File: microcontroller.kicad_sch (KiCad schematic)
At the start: 26 parts, among them IC14 PIC32MZ2048EFG064-E_PT

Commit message: first round of revisions
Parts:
- FB1, FB2, FB3, FB4: symbol SamacSys_Parts:BMC1JY0300AN -> Oro:FerriteBead
- IC14: Mouser Part Number (none) -> 579-MZ2048EFG064EPT; Mouser Price/Stock (none) -> https://www.mouser.de/ProductDetail/Microchip-Technology-At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
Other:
- moved on the sheet: FB1, FB2, FB3, FB4
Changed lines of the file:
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@@
+    (stroke (width 0) (type default))
+  )
+  (wire (pts (xy 256.54 93.98) (xy 267.97 93.98))
     (stroke (width 0) (type default))
   )
@@
     (stroke (width 0) (type default))
   )
-  (wire (pts (xy 215.9 93.98) (xy 224.79 93.98))
+  (wire (pts (xy 213.36 93.98) (xy 224.79 93.98))
     (stroke (width 0) (type default))
   )
@@
     (stroke (width 0) (type default))
   )
-  (wire (pts (xy 243.84 113.03) (xy 243.84 119.38))
+  (wire (pts (xy 243.84 110.49) (xy 243.84 119.38))
     (stroke (width 0) (type default))
   )
@@
     (stroke (width 0) (type default))
   )
-  (wire (pts (xy 200.66 113.03) (xy 200.66 119.38))
+  (wire (pts (xy 200.66 110.49) (xy 200.66 119.38))
     (stroke (width 0) (type default))
   )
@@
     (stroke (width 0) (type default))
   )
-  (wire (pts (xy 259.08 93.98) (xy 267.97 93.98))
-    (stroke (width 0) (type default))
-  )
   (wire (pts (xy 100.33 31.75) (xy 100.33 36.83))
     (stroke (width 0) (type default))
@@
     (fill (type none))
   )
+  (arc (start 248.92 99.06) (mid 249.292 98.162) (end 250.19 97.79)
+    (stroke (width 0) (type default))
+    (fill (type none))
+  )
+  (arc (start 248.92 101.6) (mid 248.548 102.498) (end 247.65 102.87)
+    (stroke (width 0) (type default))
+    (fill (type none))
+  )
   (rectangle (start 134.62 173.99) (end 135.89 173.99)
     (stroke (width 0) (type default))
@@
     (fill (type none))
   )
+  (arc (start 205.74 101.6) (mid 205.368 102.498) (end 204.47 102.87)
+    (stroke (width 0) (type default))
+    (fill (type none))
+  )
   (rectangle (start 135.89 173.99) (end 135.89 191.77)
     (stroke (width 0) (type default))
@@
   )
   (rectangle (start 220.98 116.84) (end 222.25 116.84)
+    (stroke (width 0) (type default))
+    (fill (type none))
+  )
+  (arc (start 205.74 99.06) (mid 206.112 98.162) (end 207.01 97.79)
     (stroke (width 0) (type default))
     (fill (type none))
@@
   (symbol (lib_id "SamacSys_Parts:01016D104KAT2A") (at 267.97 93.98 90) (mirror x) (unit 1)
     (in_bom yes) (on_board yes) (dnp no)
-    (property "Reference" "C16" (at 271.78 100.33 90)
-      (effects (font (size 1.27 1.27)) (justify right))
-    )
-    (property "Value" "0.1u" (at 274.32 102.87 90)
-      (effects (font (size 1.27 1.27)) (justify left))
+    (property "Reference" "C16" (at 269.24 104.14 90)
+      (effects (font (size 1.27 1.27)) (justify right bottom))
+    )
+    (property "Value" "0.1u" (at 269.24 104.14 90)
+      (effects (font (size 1.27 1.27)) (justify right top))
     )
     (property "Footprint" "SamacSys_Parts:CAPC0402X22N" (at 266.7 102.87 0)
@@
     )
   )
-  (symbol (lib_name "BMC1JY0300AN_1") (lib_id "SamacSys_Parts:BMC1JY0300AN") (at 200.66 93.98 0) (unit 1)
+  (symbol (lib_id "Oro:FerriteBead") (at 200.66 93.98 0) (unit 1)
     (in_bom yes) (on_board yes) (dnp no)
-    (property "Reference" "FB1" (at 213.36 95.25 0)
-      (effects (font (size 1.27 1.27)))
-    )
-    (property "Value" "BMC1JY0300AN" (at 210.82 99.06 0)
+    (property "Reference" "FB1" (at 209.55 96.52 0)
+      (effects (font (size 1.27 1.27)))
+    )
+    (property "Value" "BMC1JY0300AN" (at 209.55 100.33 0)
       (effects (font (size 1.27 1.27)))
     )
@@
     )
   )
-  (symbol (lib_name "BMC1JY0300AN_1") (lib_id "SamacSys_Parts:BMC1JY0300AN") (at 243.84 93.98 0) (unit 1)
+  (symbol (lib_id "Oro:FerriteBead") (at 243.84 93.98 0) (unit 1)
     (in_bom yes) (on_board yes) (dnp no)
-    (property "Reference" "FB3" (at 256.54 95.25 0)
-      (effects (font (size 1.27 1.27)))
-    )
-    (property "Value" "BMC1JY0300AN" (at 254 99.06 0)
+    (property "Reference" "FB3" (at 252.73 96.52 0)
+      (effects (font (size 1.27 1.27)))
+    )
+    (property "Value" "BMC1JY0300AN" (at 252.73 100.33 0)
       (effects (font (size 1.27 1.27)))
     )
@@
   (symbol (lib_id "SamacSys_Parts:01016D104KAT2A") (at 224.79 93.98 90) (mirror x) (unit 1)
     (in_bom yes) (on_board yes) (dnp no)
-    (property "Reference" "C16" (at 228.6 100.33 90)
-      (effects (font (size 1.27 1.27)) (justify right))
-    )
-    (property "Value" "0.1u" (at 232.41 102.87 90)
-      (effects (font (size 1.27 1.27)) (justify left))
+    (property "Reference" "C16" (at 226.06 104.14 90)
+      (effects (font (size 1.27 1.27)) (justify right bottom))
+    )
+    (property "Value" "0.1u" (at 226.06 104.14 90)
+      (effects (font (size 1.27 1.27)) (justify right top))
     )
     (property "Footprint" "SamacSys_Parts:CAPC0402X22N" (at 223.52 102.87 0)
@@
     )
   )
-  (symbol (lib_name "BMC1JY0300AN_1") (lib_id "SamacSys_Parts:BMC1JY0300AN") (at 243.84 97.79 270) (unit 1)
+  (symbol (lib_id "Oro:FerriteBead") (at 243.84 97.79 270) (unit 1)
     (in_bom yes) (on_board yes) (dnp no)
-    (property "Reference" "FB4" (at 246.38 105.41 90)
-      (effects (font (size 1.27 1.27)) (justify left))
+    (property "Reference" "FB4" (at 247.65 105.41 90)
+      (effects (font (size 1.27 1.27)))
     )
     (property "Value" "BMC1JY0300AN" (at 234.4634 102.2953 90)
@@
       (effects (font (size 1.27 1.27)) (justify left) hide)
     )
-    (property "Mouser Part Number" "" (at 175.26 45.72 0)
-      (effects (font (size 1.27 1.27)) (justify left) hide)
-    )
-    (property "Mouser Price/Stock" "" (at 175.26 48.26 0)
+    (property "Mouser Part Number" "579-MZ2048EFG064EPT" (at 175.26 45.72 0)
+      (effects (font (size 1.27 1.27)) (justify left) hide)
+    )
+    (property "Mouser Price/Stock" "https://www.mouser.de/ProductDetail/Microchip-Technology-Atmel/PIC32MZ2048EFG064-E-PT?qs=r%2FmwOkjQ8utX5RH6pDxK9w%3D%3D" (at 175.26 48.26 0)
       (effects (font (size 1.27 1.27)) (justify left) hide)
     )
@@
     )
   )
-  (symbol (lib_name "BMC1JY0300AN_1") (lib_id "SamacSys_Parts:BMC1JY0300AN") (at 200.66 97.79 270) (unit 1)
+  (symbol (lib_id "Oro:FerriteBead") (at 200.66 97.79 270) (unit 1)
     (in_bom yes) (on_board yes) (dnp no)
-    (property "Reference" "FB2" (at 203.2 105.41 90)
-      (effects (font (size 1.27 1.27)) (justify left))
+    (property "Reference" "FB2" (at 204.47 105.41 90)
+      (effects (font (size 1.27 1.27)))
     )
     (property "Value" "BMC1JY0300AN" (at 191.2834 102.2953 90)

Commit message: begin refactor for rev3
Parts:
- added C16 (x8): 0.1u, SamacSys_Parts:CAPC0402X22N, symbol SamacSys_Parts:01016D104KAT2A
- added C21: 1u, SamacSys_Parts:CAPC1608X90N, symbol SamacSys_Parts:0603YD105KAT2A
- added C22: 4.7u, SamacSys_Parts:CAPC2012X135N, symbol SamacSys_Parts:CL21A475KOFNNNE
- added C68, C69, C71: 2.2u, CAPC1608X90N, symbol SamacSys_Parts:CL10A225KP8NNNC
- added IC8: STM32F479VGT6, QFP50P1600X1600X160-100N, symbol SamacSys_Parts:STM32F479VGT6
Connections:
- net VDD1 is gone; now on net +3V3: C16.2, C16.2, C16.2, FB2.2, IC14.54 (VDD_4), IC14.60 (VDD_5), IC14.8 (VDD_1)
- net VDD2 is gone; now on net +3V3: C16.2, C16.2, C16.2, FB4.2, IC14.26 (VDD_2), IC14.34 (VUSB3V3), IC14.39 (VDD_3)
- net +3V3: now also C16.2, C16.2, C16.2, C16.2, C16.2, C16.2, C16.2, C16.2, C21.2, C22.1, C71.1, IC8.100 (VDD_5), IC8.17 (VREF+), IC8.18 (VDDA), IC8.24 (VDD_2), IC8.3 (VBAT), IC8.45 (VDD_3), IC8.55 (VDDDSI), IC8.56 (VCAPDSI), IC8.62 (VDD12DSI), IC8.65 (VDDUSB), IC8.77 (VDD_4), IC8.8 (VDD_1)
- net ETH_~{RST}: now also IC8.4 (PC13)
- net GND: now also C16.1, C16.1, C16.1, C16.1, C16.1, C16.1, C16.1, C16.1, C21.1, C22.2, C68.2, C69.2, C71.2, IC8.16 (VSSA), IC8.2 (VSS_1), IC8.23 (VSS_3), IC8.44 (VSS_4), IC8.59 (VSSDSI), IC8.7 (VSS_2), IC8.78 (VSS_5)
- new net VCAP1: C68.1, IC8.43 (VCAP1)
- new net VCAP2: C69.1, IC8.76 (VCAP2)
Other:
- note added: "TODO: OSCILLATOR"
- moved on the sheet: C16, FB1, FB2, FB3, FB4, IC14, R19, R43

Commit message: fully move to new MCU configuration
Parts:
- removed C16 (x10): 0.1u, SamacSys_Parts:CAPC0402X22N, symbol SamacSys_Parts:01016D104KAT2A
- removed FB1, FB2, FB3, FB4: BMC1JY0300AN, BEADC1608X95N, symbol Oro:FerriteBead
- removed IC14: PIC32MZ2048EFG064-E_PT, SamacSys_Parts:QFP50P1200X1200X120-64N, symbol SamacSys_Parts:PIC32MZ2048EFG064-E_PT
- removed R43 (x9): 10k, RESC5025X65N, symbol SamacSys_Parts:RC2010JK-0710KL
- added LED5: AA3528VRVFS/A, SamacSys_Parts:AA3528VRVFSA, symbol SamacSys_Parts:AA3528VRVFS_A
- added R10: 10k, SamacSys_Parts:RESC5025X65N, symbol SamacSys_Parts:RC2010JK-0710KL
- added R5: 1k, RESC2012X60N, symbol SamacSys_Parts:SG73P2ATTD102J
- renumbered C71 to C11, C68 to C2, C69 to C3, IC8 to IC1, R19 to R1, R19 to R2
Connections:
- net ETH_~{RST} is gone; now on net EXTETH_~{RST}: IC1.4 (PC13)
- net +3V3: now also LED5.2, R10.1
- net EXTETH_SCK: now also IC1.41 (PB10)
- net I2C_SCL: now also IC1.95 (PB6)
- net I2C_SDA: now also IC1.96 (PB7)
- net OLED_SCK: now also IC1.81 (PC10)
- net OLED_~{RST}: now also IC1.89 (PD5)
- net USB_D+: now also IC1.74 (PA12)
- net USB_D-: now also IC1.73 (PA11)
- net EXTETH_MISO: now reaches IC1.14 (PC2)
- net EXTETH_MOSI: now reaches IC1.15 (PC3)
- net SYSUART_RTS: now reaches IC1.20 (PA1)
- net SYSUART_TX: now reaches IC1.21 (PA2)
- net SYSUART_RX: now reaches IC1.22 (PA3)
- net SYSETH_SCK: now reaches IC1.26 (PA5)
- net SYSETH_MISO: now reaches IC1.27 (PA6)
- net SYSTEH_MOSI: now reaches IC1.28 (PA7)
- net SYSTEH_~{RST}: now reaches IC1.29 (PB0)
- net SYSTEH_~{INT}: now reaches IC1.30 (PB1)
- net DBGUART_RX: now reaches IC1.32 (PE7)
- net DBGUART_TX: now reaches IC1.33 (PE8)
- net at IC1.37 (PE12): now also R5.1
- net PSU_ON: now reaches IC1.47 (PB13)
- net PSU_OK: now reaches IC1.48 (PB14)
- net SYS_RESET: now reaches IC1.49 (PB15)
- net SYS_POWER: now reaches IC1.50 (PD8)
- net SWDIO: now reaches IC1.75 (PA13)
- net SWCLK: now reaches IC1.79 (PA14)
- net SYSUART_CTS: now reaches IC1.87 (PD3)
- net OLED_MOSI: now reaches IC1.90 (PD6)
- net SWO: now reaches IC1.92 (PB3)
- net ~{FLASH}: now reaches IC1.97 (BOOT0)
- net ~{FLASH}: now also R10.2
- net EXTETH_~{INT}: now reaches IC1.99 (PB9)
- new net: LED5.1, R5.2
- no-connect marks 0 -> 44
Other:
- note removed: "10k"
- moved on the sheet: R1, R2

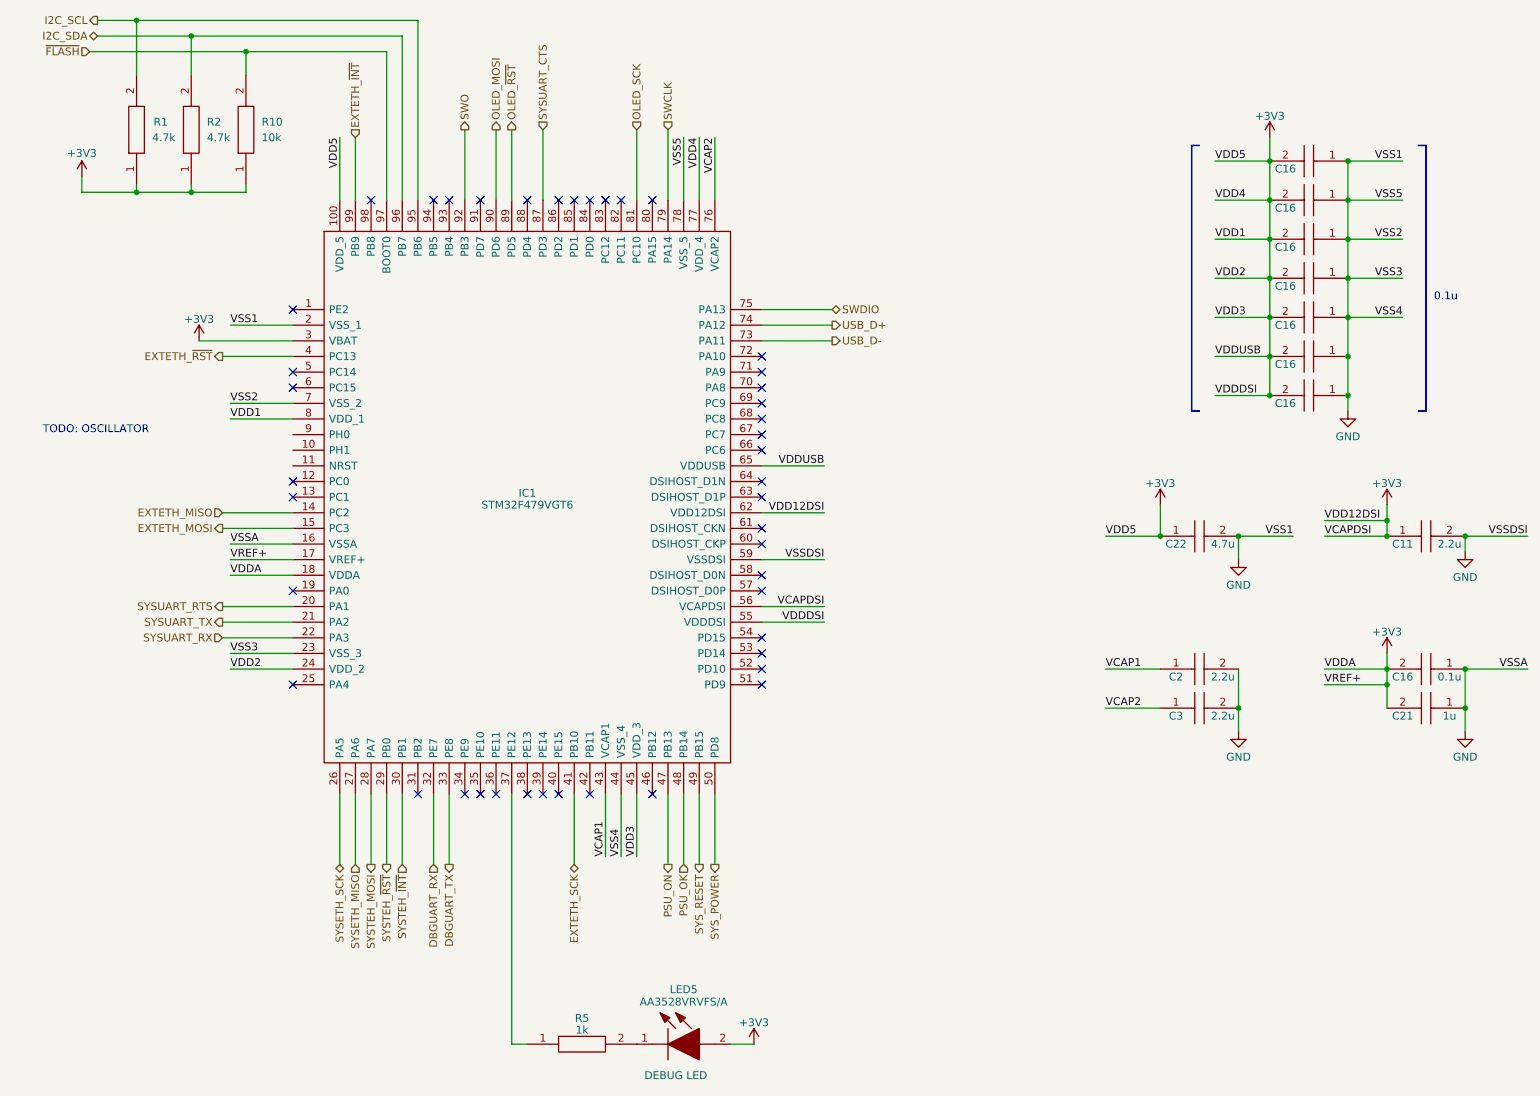
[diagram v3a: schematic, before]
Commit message: first few boards laid out
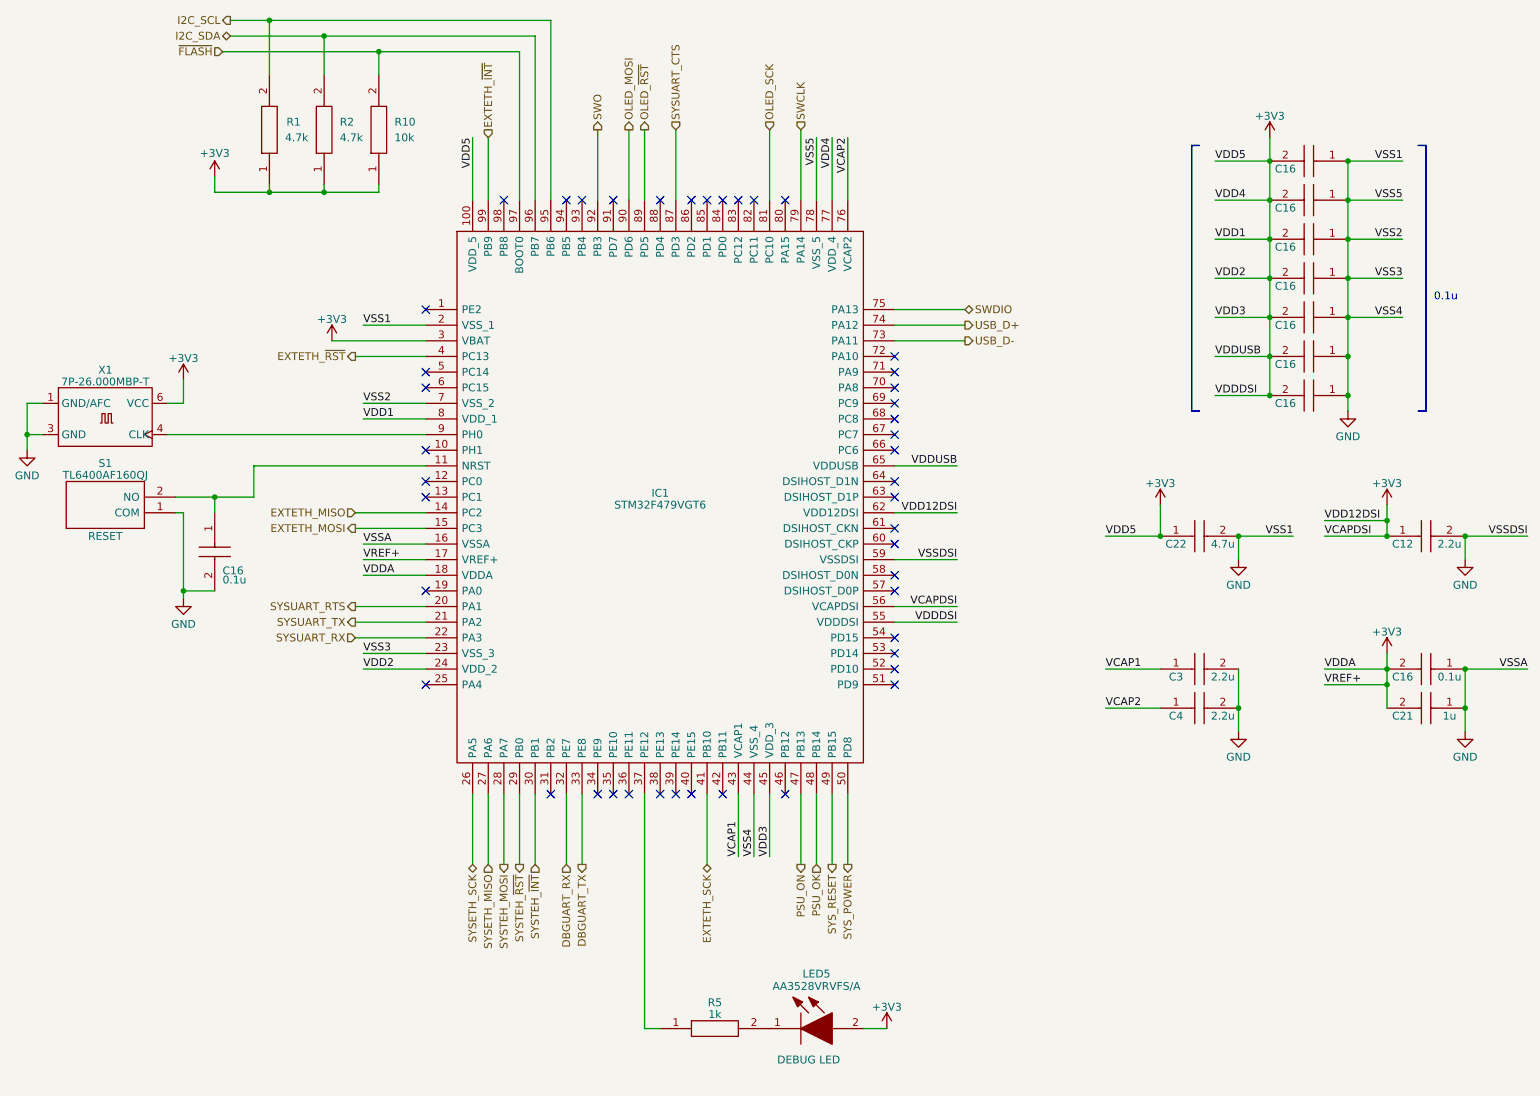
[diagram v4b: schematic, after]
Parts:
- added C16: 0.1u, SamacSys_Parts:CAPC0402X22N, symbol SamacSys_Parts:GRT31C5C1H104FA02L
- added S1: TL6400AF160QJ, TL6400AF160QJ, symbol SamacSys_Parts:TL6400AF160QJ
- added X1: 7P-26.000MBP-T, Oro Footprints:7P-26.000MBP-T, symbol Oro:7P-26.000MBP-T
- C16: symbol SamacSys_Parts:01016D104KAT2A -> SamacSys_Parts:GRT31C5C1H104FA02L
- R1, R2: symbol SamacSys_Parts:MCWR04X4701FTL -> SamacSys_Parts:RC2512FK-074K7L; Arrow Part Number (none) -> RC2512FK-074K7L; Arrow Price/Stock (none) -> https://www.arrow.com/en/products/rc2512fk-074k7l/yageo?reg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; Mouser Part Number (none) -> 603-RC2512FK-074K7L; Mouser Price/Stock (none) -> https://www.mouser.co.uk/ProductDetail/YAGEO/RC2512FK-074K7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
- renumbered C11 to C12, C2 to C3, C3 to C4
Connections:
- net +3V3: now also X1.6 (VCC)
- net GND: now also C16.2, S1.1 (COM), X1.1 (GND/AFC), X1.3 (GND)
- net at IC1.11 (NRST): now also C16.1, S1.2 (NO)
- net at IC1.9 (PH0): now also X1.4 (CLK)
- no-connect marks 44 -> 45
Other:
- note removed: "TODO: OSCILLATOR"
- moved on the sheet: IC1, LED5, R1, R10, R2, R5
